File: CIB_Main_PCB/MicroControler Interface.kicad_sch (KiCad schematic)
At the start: 4 parts

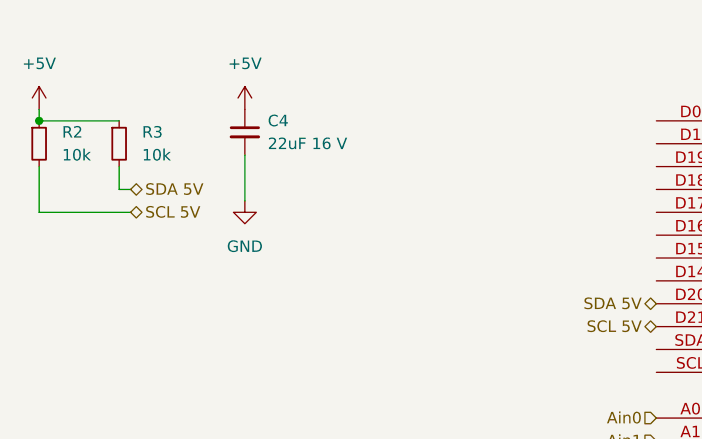
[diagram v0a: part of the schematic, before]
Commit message: added snubbing to the relays
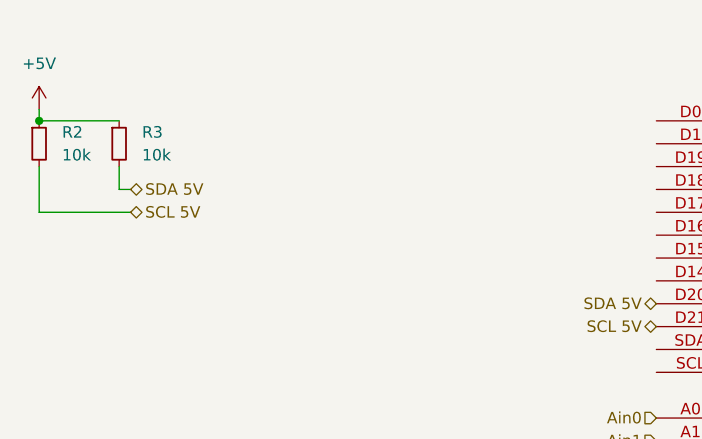
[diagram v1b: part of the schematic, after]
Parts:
- removed C4: 22uF 16 V, Capacitor_SMD:C_1206_3216Metric_Pad1.33x1.80mm_HandSolder, symbol Device:C_Small
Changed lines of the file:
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@@
-    (stroke (width 0) (type default) (color 0 0 0 0))
-  )
-  (wire (pts (xy 40.64 29.21) (xy 40.64 34.29))
     (stroke (width 0) (type default) (color 0 0 0 0))
   )
@@
       (effects (font (size 1.27 1.27)) hide)
     )
-    (pin "1")
-  )
-  (symbol (lib_id "power:GND") (at 40.64 34.29 0) (unit 1)
-    (in_bom yes) (on_board yes) (fields_autoplaced)
-    (property "Reference" "#PWR016" (id 0) (at 40.64 40.64 0)
-      (effects (font (size 1.27 1.27)) hide)
-    )
-    (property "Value" "GND" (id 1) (at 40.64 39.37 0))
-    (property "Footprint" "" (id 2) (at 40.64 34.29 0)
-      (effects (font (size 1.27 1.27)) hide)
-    )
-    (property "Datasheet" "" (id 3) (at 40.64 34.29 0)
-      (effects (font (size 1.27 1.27)) hide)
-    )
-    (pin "1")
-  )
-  (symbol (lib_id "Device:C_Small") (at 40.64 26.67 0) (unit 1)
-    (in_bom yes) (on_board yes) (fields_autoplaced)
-    (property "Reference" "C4" (id 0) (at 43.18 25.4062 0)
-      (effects (font (size 1.27 1.27)) (justify left))
-    )
-    (property "Value" "22uF 16 V" (id 1) (at 43.18 27.9462 0)
-      (effects (font (size 1.27 1.27)) (justify left))
-    )
-    (property "Footprint" "Capacitor_SMD:C_1206_3216Metric_Pad1.33x1.80mm_HandSolder" (id 2) (at 40.64 26.67 0)
-      (effects (font (size 1.27 1.27)) hide)
-    )
-    (property "Datasheet" "https://www.we-online.com/katalog/datasheet/885012108018.pdf" (id 3) (at 40.64 26.67 0)
-      (effects (font (size 1.27 1.27)) hide)
-    )
-    (property "Manufacturer #" "885012108018" (id 4) (at 40.64 26.67 0)
-      (effects (font (size 1.27 1.27)) hide)
-    )
-    (property "DigiKey #" "732-7642-1-ND" (id 5) (at 40.64 26.67 0)
-      (effects (font (size 1.27 1.27)) hide)
-    )
-    (property "Manufacturer" "Würth Elektronik" (id 6) (at 40.64 26.67 0)
-      (effects (font (size 1.27 1.27)) hide)
-    )
-    (property "Description" "22 µF ±20% 16V Ceramic Capacitor X5R 1206 (3216 Metric)" (id 7) (at 40.64 26.67 0)
-      (effects (font (size 1.27 1.27)) hide)
-    )
-    (property "DigiKey Price/Stock" "https://www.digikey.co.uk/en/products/detail/w%C3%BCrth-elektronik/885012108018/5453497?s=N4IgTCBcDaIOwGYwFo4DYAsKCMyByAIiALoC%2BQA" (id 8) (at 40.64 26.67 0)
-      (effects (font (size 1.27 1.27)) hide)
-    )
-    (pin "1")
-    (pin "2")
-  )
-  (symbol (lib_id "power:+5V") (at 40.64 24.13 0) (unit 1)
-    (in_bom yes) (on_board yes) (fields_autoplaced)
-    (property "Reference" "#PWR014" (id 0) (at 40.64 27.94 0)
-      (effects (font (size 1.27 1.27)) hide)
-    )
-    (property "Value" "+5V" (id 1) (at 40.64 19.05 0))
-    (property "Footprint" "" (id 2) (at 40.64 24.13 0)
-      (effects (font (size 1.27 1.27)) hide)
-    )
-    (property "Datasheet" "" (id 3) (at 40.64 24.13 0)
-      (effects (font (size 1.27 1.27)) hide)
-    )
